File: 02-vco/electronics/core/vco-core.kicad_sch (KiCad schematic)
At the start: 7 parts, among them J1 Conn_01x04, J2 Conn_02x05_Odd_Even, J6 Conn_02x02_Counter_Clockwise

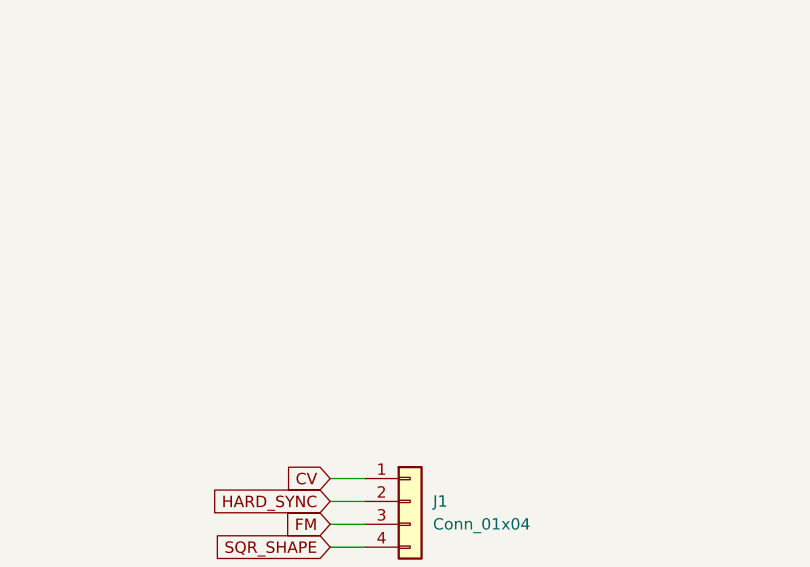
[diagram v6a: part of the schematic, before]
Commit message: Added default IO conn. to VCO core
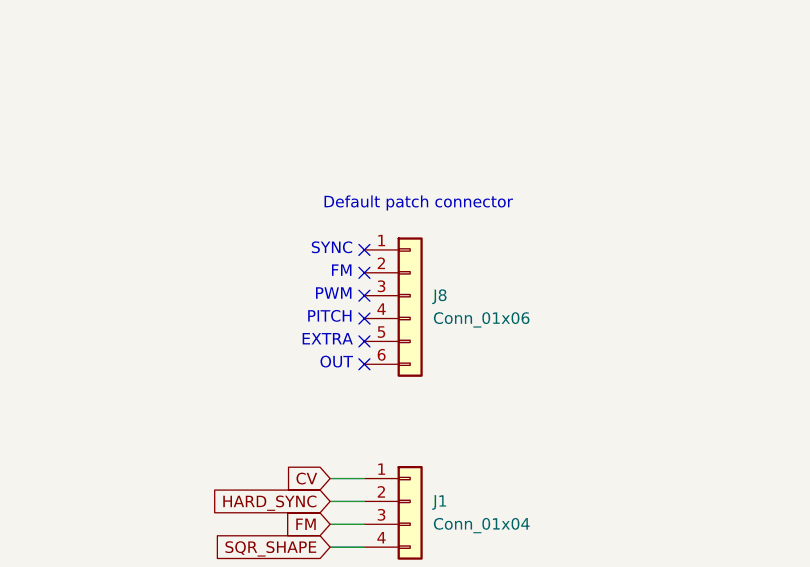
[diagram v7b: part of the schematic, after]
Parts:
- added J8: Conn_01x06, Connector_PinHeader_2.54mm:PinHeader_1x06_P2.54mm_Vertical, symbol Connector_Generic:Conn_01x06
- J1: footprint Connector_PinSocket_2.54mm:PinSocket_1x04_P2.54mm_Vertical -> Connector_PinHeader_2.54mm:PinHeader_1x04_P2.54mm_Vertical
- J2: footprint Connector_PinSocket_2.54mm:PinSocket_2x05_P2.54mm_Vertical -> Connector_PinHeader_2.54mm:PinHeader_2x05_P2.54mm_Vertical
- J6: footprint Connector_PinSocket_2.54mm:PinSocket_2x02_P2.54mm_Vertical -> Connector_PinHeader_2.54mm:PinHeader_2x02_P2.54mm_Vertical; now left out of the parts list
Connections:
- no-connect marks 0 -> 6
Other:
- note added: "Default patch connector"
- note added: "EXTRA"
- note added: "FM"
- note added: "OUT"
- note added: "PITCH"
- note added: "PWM"
- note added: "SYNC"
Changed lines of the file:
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@@
+		)
+	)
+	(text "PWM"
+		(exclude_from_sim no)
+		(at 209.55 58.42 0)
+		(effects
+			(font
+				(size 1.27 1.27)
+			)
+			(justify right)
+		)
+	)
+	(text "Default patch connector"
+		(exclude_from_sim no)
+		(at 227.33 48.26 0)
+		(effects
+			(font
+				(size 1.27 1.27)
+			)
+			(justify right)
+		)
+	)
+	(text "OUT"
+		(exclude_from_sim no)
+		(at 209.55 66.04 0)
+		(effects
+			(font
+				(size 1.27 1.27)
+			)
+			(justify right)
+		)
+	)
+	(text "SYNC"
+		(exclude_from_sim no)
+		(at 209.55 53.34 0)
+		(effects
+			(font
+				(size 1.27 1.27)
+			)
+			(justify right)
 		)
 	)
@@
 			)
 			(justify left)
+		)
+	)
+	(text "EXTRA"
+		(exclude_from_sim no)
+		(at 209.55 63.5 0)
+		(effects
+			(font
+				(size 1.27 1.27)
+			)
+			(justify right)
 		)
 	)
@@
 		)
 	)
+	(text "FM"
+		(exclude_from_sim no)
+		(at 209.55 55.88 0)
+		(effects
+			(font
+				(size 1.27 1.27)
+			)
+			(justify right)
+		)
+	)
 	(text "I/O"
 		(exclude_from_sim no)
@@
 			)
 			(justify left)
+		)
+	)
+	(text "PITCH"
+		(exclude_from_sim no)
+		(at 209.55 60.96 0)
+		(effects
+			(font
+				(size 1.27 1.27)
+			)
+			(justify right)
 		)
 	)
@@
 		(color 0 0 0 0)
 	)
+	(no_connect
+		(at 210.82 66.04)
+	)
+	(no_connect
+		(at 210.82 53.34)
+	)
+	(no_connect
+		(at 210.82 60.96)
+	)
+	(no_connect
+		(at 210.82 55.88)
+	)
+	(no_connect
+		(at 210.82 63.5)
+	)
+	(no_connect
+		(at 210.82 58.42)
+	)
 	(wire
 		(pts
@@
 		(unit 1)
 		(exclude_from_sim no)
-		(in_bom yes)
+		(in_bom no)
 		(on_board yes)
 		(dnp no)
@@
 			)
 		)
-		(property "Footprint" "Connector_PinSocket_2.54mm:PinSocket_2x02_P2.54mm_Vertical"
+		(property "Footprint" "Connector_PinHeader_2.54mm:PinHeader_2x02_P2.54mm_Vertical"
 			(at 252.73 101.6 0)
 			(effects
@@
 			)
 		)
-		(property "Footprint" "Connector_PinSocket_2.54mm:PinSocket_1x04_P2.54mm_Vertical"
+		(property "Footprint" "Connector_PinHeader_2.54mm:PinHeader_1x04_P2.54mm_Vertical"
 			(at 215.9 81.28 0)
 			(effects
@@
 	)
 	(symbol
+		(lib_id "Connector_Generic:Conn_01x06")
+		(at 215.9 58.42 0)
+		(unit 1)
+		(exclude_from_sim no)
+		(in_bom yes)
+		(on_board yes)
+		(dnp no)
+		(fields_autoplaced yes)
+		(property "Reference" "J8"
+			(at 218.44 58.4199 0)
+			(effects
+				(font
+					(size 1.27 1.27)
+				)
+				(justify left)
+			)
+		)
+		(property "Value" "Conn_01x06"
+			(at 218.44 60.9599 0)
+			(effects
+				(font
+					(size 1.27 1.27)
+				)
+				(justify left)
+			)
+		)
+		(property "Footprint" "Connector_PinHeader_2.54mm:PinHeader_1x06_P2.54mm_Vertical"
+			(at 215.9 58.42 0)
+			(effects
+				(font
+					(size 1.27 1.27)
+				)
+				(hide yes)
+			)
+		)
+		(property "Datasheet" "~"
+			(at 215.9 58.42 0)
+			(effects
+				(font
+					(size 1.27 1.27)
+				)
+				(hide yes)
+			)
+		)
+		(property "Description" "Generic connector, single row, 01x06, script generated (kicad-library-utils/schlib/autogen/connector/)"
+			(at 215.9 58.42 0)
+			(effects
+				(font
+					(size 1.27 1.27)
+				)
+				(hide yes)
+			)
+		)
+		(property "Part No." ""
+			(at 215.9 58.42 0)
+			(effects
+				(font
+					(size 1.27 1.27)
+				)
+				(hide yes)
+			)
+		)
+		(property "Part URL" ""
+			(at 215.9 58.42 0)
+			(effects
+				(font
+					(size 1.27 1.27)
+				)
+				(hide yes)
+			)
+		)
+		(property "Vendor" ""
+			(at 215.9 58.42 0)
+			(effects
+				(font
+					(size 1.27 1.27)
+				)
+				(hide yes)
+			)
+		)
+		(property "LCSC" ""
+			(at 215.9 58.42 0)
+			(effects
+				(font
+					(size 1.27 1.27)
+				)
+				(hide yes)
+			)
+		)
+		(pin "5"
+		)
+		(pin "3"
+		)
+		(pin "6"
+		)
+		(pin "1"
+		)
+		(pin "4"
+		)
+		(pin "2"
+		)
+		(instances
+			(project ""
+				(path "/8e2e31f3-eed5-4de1-966c-f4162758c735"
+					(reference "J8")
+					(unit 1)
+				)
+			)
+		)
+	)
+	(symbol
 		(lib_id "power:GND")
 		(at 245.11 105.41 0)
@@
 			)
 		)
-		(property "Footprint" "Connector_PinSocket_2.54mm:PinSocket_2x05_P2.54mm_Vertical"
+		(property "Footprint" "Connector_PinHeader_2.54mm:PinHeader_2x05_P2.54mm_Vertical"
 			(at 215.9 106.68 0)
 			(effects

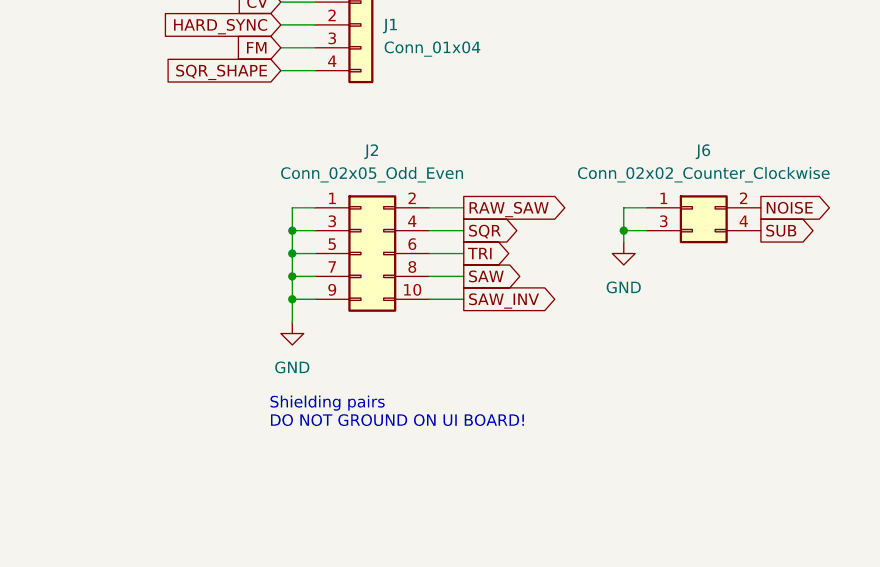
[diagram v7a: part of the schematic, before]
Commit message: Updated VCO core to use pin headers not sockets
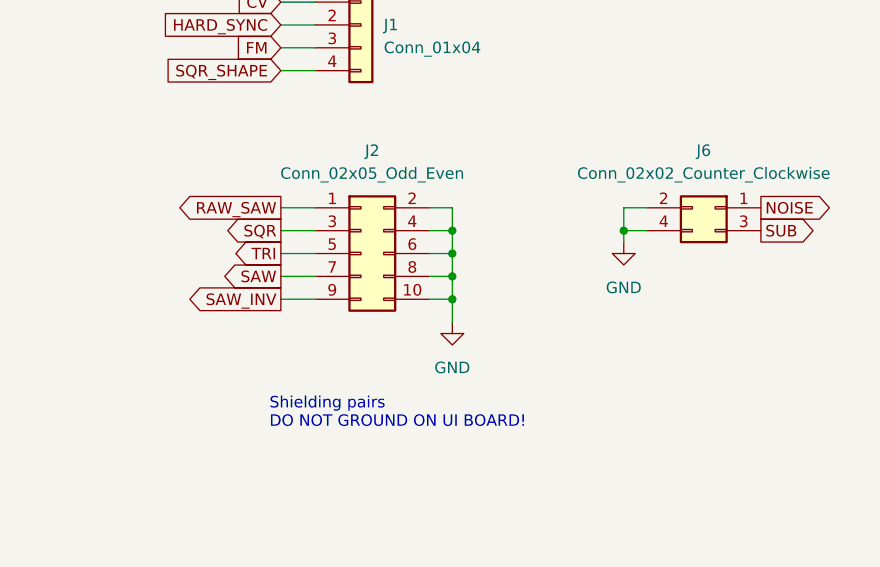
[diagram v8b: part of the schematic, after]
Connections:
- net GND: now also J2.10 (Pin_10), J2.2 (Pin_2), J2.4 (Pin_4), J2.6 (Pin_6), J2.8 (Pin_8), J6.2 (Pin_2), J6.4 (Pin_4); no longer J2.1 (Pin_1), J2.3 (Pin_3), J2.5 (Pin_5), J2.7 (Pin_7), J2.9 (Pin_9), J6.1 (Pin_1), J6.3 (Pin_3)
- net NOISE: now also J6.1 (Pin_1); no longer J6.2 (Pin_2)
- net RAW_SAW: now also J2.1 (Pin_1); no longer J2.2 (Pin_2)
- net SAW: now also J2.7 (Pin_7); no longer J2.8 (Pin_8)
- net SAW_INV: now also J2.9 (Pin_9); no longer J2.10 (Pin_10)
- net SQR: now also J2.3 (Pin_3); no longer J2.4 (Pin_4)
- net SUB: now also J6.3 (Pin_3); no longer J6.4 (Pin_4)
- net TRI: now also J2.5 (Pin_5); no longer J2.6 (Pin_6)
